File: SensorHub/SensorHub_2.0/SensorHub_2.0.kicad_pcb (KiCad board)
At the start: 2 copper layers, 30 x 28 mm, 68 parts, among them J1 Conn_01x02, J2 658561423020, J3 658561423020, J4 USB_C_Receptacle, U1 R7FA4E2B93CFM#AA0, U2 MYRGM080200C41RA, U3 TJA1051TK-3, U4 BMI270, U5 ASCODV-24.000MHZ-LR-T3

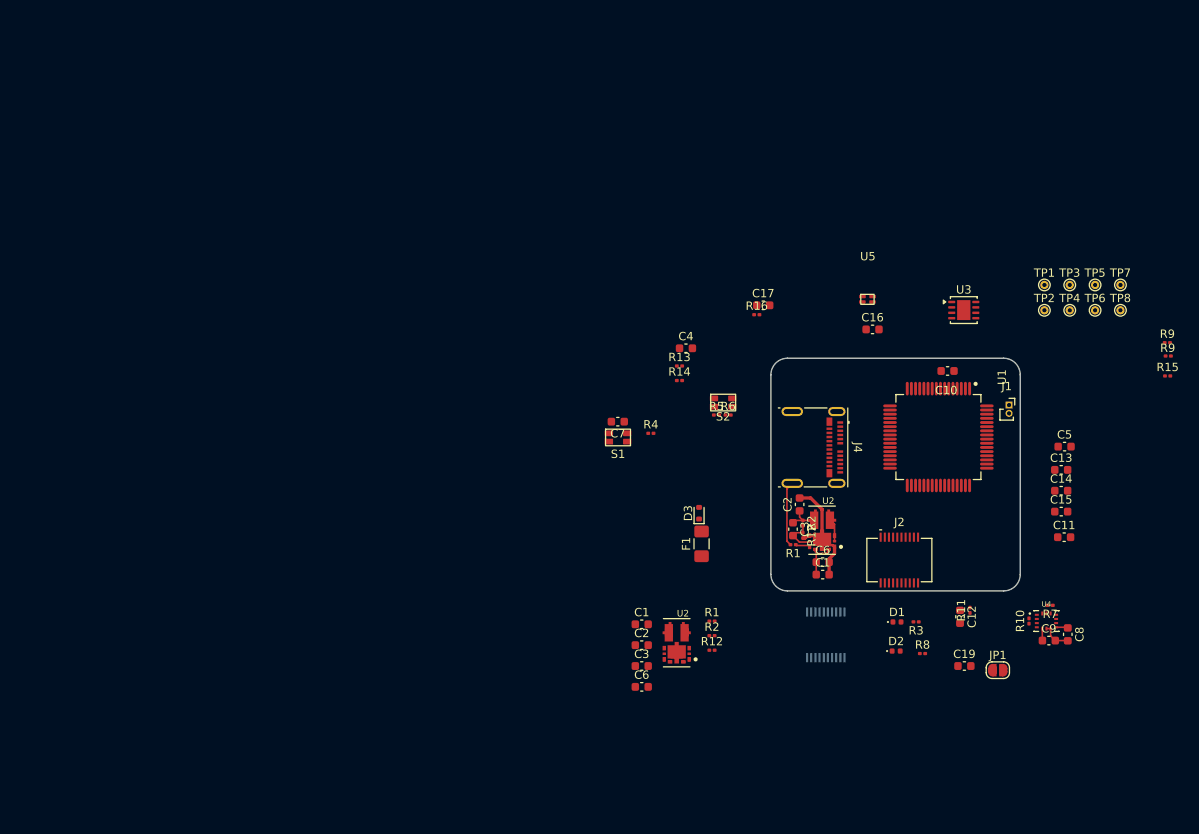
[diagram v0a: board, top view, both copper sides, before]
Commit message: 32k oscillator
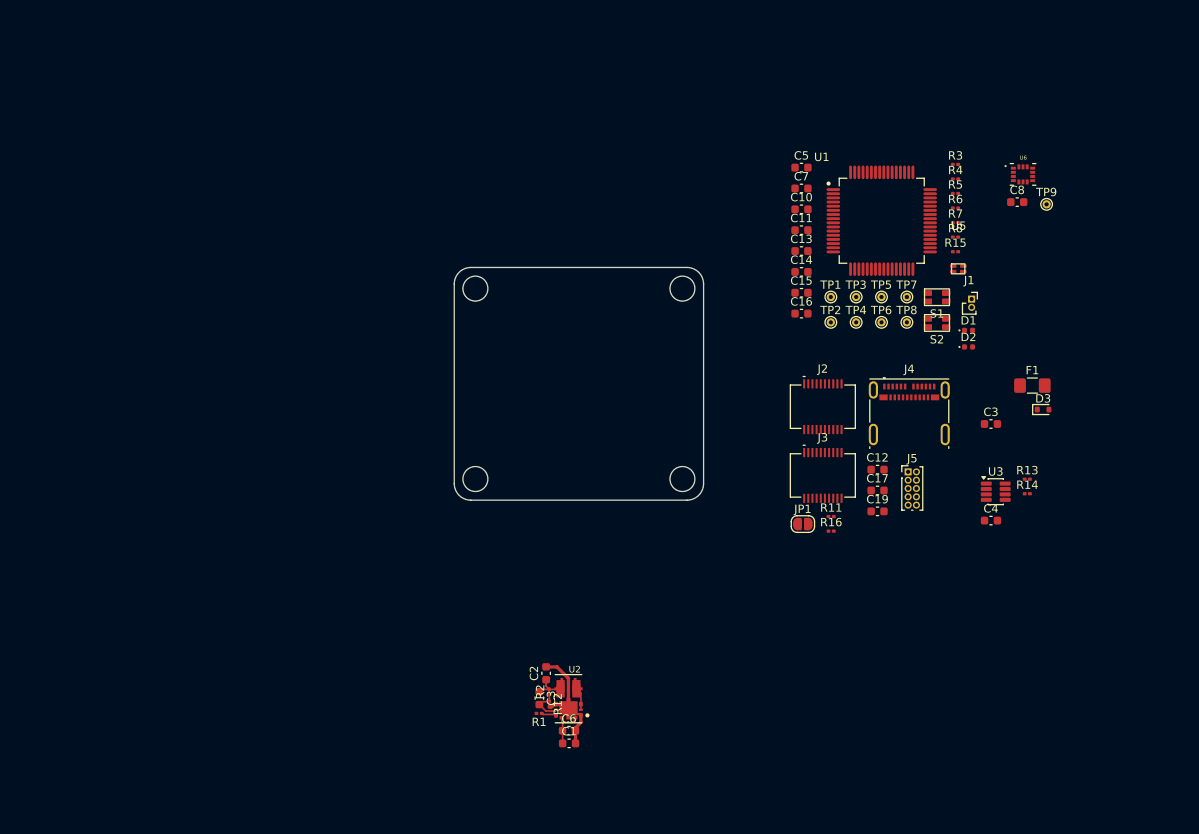
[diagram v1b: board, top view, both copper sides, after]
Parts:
- removed the C1 at (109.4, 129.6)
- removed the C1 at (131.2, 123.6)
- removed the C2 at (109.4, 132.1)
- removed the C2 at (128.4, 115.2)
- removed the C6 at (131.2, 122.1)
- removed the C6 at (109.4, 137.1)
- removed C9: 0.1 uF, Capacitor_SMD:C_0603_1608Metric
- removed the R1 at (127.6, 120.0)
- removed the R1 at (117.9, 129.2)
- removed R10, R9 (x2): 4.7 K, Resistor_SMD:R_0201_0603Metric
- removed the R12 at (117.9, 132.7)
- removed the R12 at (128.8, 118.9)
- removed the R2 at (117.9, 130.9)
- removed the R2 at (128.8, 117.4)
- removed the U2 at (131.1, 118.3)
- removed U4: BMI270, BMI270:XDCR_BMI270
- added C1: 10V/22uF, Capacitor_SMD:C_0603_1608Metric, F.Cu at (100.7, 143.9)
- added C2: 10V/22uF, Capacitor_SMD:C_0603_1608Metric, F.Cu at (97.9, 135.5)
- added C6: 16V/1uF, Capacitor_SMD:C_0603_1608Metric, F.Cu at (100.7, 142.4)
- added J5: Conn_02x05_Top_Bottom, Connector_PinHeader_1.00mm:PinHeader_2x05_P1.00mm_Vertical, F.Cu at (141.5, 111.2)
- added R1: 10 K, Resistor_SMD:R_0201_0603Metric, F.Cu at (97.1, 140.3)
- added R12: 15 K, Resistor_SMD:R_0201_0603Metric, F.Cu at (98.3, 139.2)
- added R2: 47 K, Resistor_SMD:R_0201_0603Metric, F.Cu at (98.3, 137.7)
- added TP9: TestPoint, TestPoint:TestPoint_THTPad_D1.0mm_Drill0.5mm, F.Cu at (158.1, 79.0)
- added U6: LSM6DSM, LSM6DSM:PQFN50P300X250X86-14N, F.Cu at (155.3, 75.5)
- J3: moved to F.Cu
- U3: value TJA1051TK-3 -> TCAN334; footprint Package_SON:HVSON-8-1EP_3x3mm_P0.65mm_EP1.6x2.4mm -> Package_TO_SOT_SMD:TSOT-23-8
- moved R3 55.2 mm to (147.2, 74.2), turned to 0 degrees
- moved C8 52.4 mm to (154.6, 78.8), turned to 0 degrees
- moved C3 51.1 mm to (151.4, 105.5)
- moved R8 50.3 mm to (147.2, 83.0)
- moved C11 48.6 mm to (128.6, 82.2)
- moved R4 47.7 mm to (147.2, 76.0)
- moved R7 47.4 mm to (147.2, 81.2), turned to 0 degrees
- moved C5 46.1 mm to (128.6, 74.6)
- moved F1 44.1 mm to (156.4, 100.9), turned to 0 degrees
- moved R13 44.0 mm to (155.8, 112.1)
- moved R14 44.0 mm to (155.8, 113.9)
- moved D3 43.2 mm to (157.7, 103.7), turned to 0 degrees
- moved C4 42.2 mm to (151.4, 117.1)
- moved S1 41.9 mm to (144.9, 89.7)
- moved C13 40.9 mm to (128.6, 84.7)
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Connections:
- net /Boot renamed /RA4E2_microcontroller/Boot
- net /EXTAL renamed /RA4E2_microcontroller/EXTAL
- net /LED1 renamed /RA4E2_microcontroller/LED1
- net /LED2 renamed /RA4E2_microcontroller/LED2
- net /SWCLK renamed /RA4E2_microcontroller/SWCLK
- net /SWDIO renamed /RA4E2_microcontroller/SWDIO
- net /VCL renamed /RA4E2_microcontroller/VCL
- C16 pad 1: +3.3V -> unconnected-(C16-Pad1)
- C4 pad 2: unconnected-(C4-Pad2) -> GND
- J2 pad 1: unconnected-(J2-Pad1) -> GND
- J2 pad 10: unconnected-(J2-Pad10) -> GND
- J2 pad 11: unconnected-(J2-Pad11) -> GND
- J2 pad 12: unconnected-(J2-Pad12) -> /SCL_0
- J2 pad 13: unconnected-(J2-Pad13) -> GND
- J2 pad 14: unconnected-(J2-Pad14) -> /SDA_0
- J2 pad 15: unconnected-(J2-Pad15) -> GND
- J2 pad 16: unconnected-(J2-Pad16) -> /CS
- J2 pad 17: unconnected-(J2-Pad17) -> /SCK
- J2 pad 18: unconnected-(J2-Pad18) -> /MOSI
- J2 pad 19: unconnected-(J2-Pad19) -> /MISO
- J2 pad 2: unconnected-(J2-Pad2) -> /+3.3V
- J2 pad 20: unconnected-(J2-Pad20) -> GND
- J2 pad 3: unconnected-(J2-Pad3) -> GND
- J2 pad 4: unconnected-(J2-Pad4) -> /Analog
- J2 pad 5: unconnected-(J2-Pad5) -> GND
- J2 pad 6: unconnected-(J2-Pad6) -> /INT2
- J2 pad 7: unconnected-(J2-Pad7) -> /GP1
- J2 pad 8: unconnected-(J2-Pad8) -> GND
- J2 pad 9: unconnected-(J2-Pad9) -> /+5V
- J3 pad 1: unconnected-(J3-Pad1) -> GND
- J3 pad 10: unconnected-(J3-Pad10) -> GND
- J3 pad 11: unconnected-(J3-Pad11) -> GND
- J3 pad 12: unconnected-(J3-Pad12) -> /SCL_0
- J3 pad 13: unconnected-(J3-Pad13) -> GND
- J3 pad 14: unconnected-(J3-Pad14) -> /SDA_0
- J3 pad 15: unconnected-(J3-Pad15) -> GND
- J3 pad 16: unconnected-(J3-Pad16) -> /CS
- J3 pad 17: unconnected-(J3-Pad17) -> /SCK
- J3 pad 18: unconnected-(J3-Pad18) -> /MOSI
- J3 pad 19: unconnected-(J3-Pad19) -> /MISO
- J3 pad 2: unconnected-(J3-Pad2) -> /+3.3V
- J3 pad 20: unconnected-(J3-Pad20) -> GND
- J3 pad 3: unconnected-(J3-Pad3) -> GND
- J3 pad 4: unconnected-(J3-Pad4) -> /Analog
- J3 pad 5: unconnected-(J3-Pad5) -> GND
- J3 pad 6: unconnected-(J3-Pad6) -> /INT2
- J3 pad 7: unconnected-(J3-Pad7) -> /GP1
- J3 pad 8: unconnected-(J3-Pad8) -> GND
- J3 pad 9: unconnected-(J3-Pad9) -> /+5V
- R15 pad 2: /SDA_0 -> /SDL_0
- TP4 pad 1: /SDA_0 -> /SDL_0
- U1 pad 12: /TX+ -> unconnected-(U1-P411-Pad12)
- U1 pad 14: /GPIO -> /GP1
- U1 pad 28: /INT2 -> unconnected-(U1-P304-Pad28)
- U1 pad 34: /MISO/SCL -> /MISO
- U1 pad 35: /MOSI/SDA -> /MOSI
- U1 pad 4: /SDA_0 -> /SDL_0
- U2 pad 6: /MYRGM080200C41RA +5\+3.3/Sleep -> /Sleep
- U3 pad 2: Net-(U3-GND-Pad2) -> GND
- U3 pad 3: +5V -> +3.3V
- U3 pad 5: +3.3V -> GND
- U3 pad 8: unconnected-(U3-S-Pad8) -> GND
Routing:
- net GND: track 26.5 -> 16.9 mm
- net +3.3V: track 6.97 -> 4.09 mm
- net /MYRGM080200C41RA +5\+3.3/LX: track 0.00 -> 2.79 mm
- net /LX: track 2.79 -> 0.00 mm
- net unconnected-(U2-2_NC-Pad4): track 1.22 -> 0.00 mm
- net unconnected-(U2-1_NC-Pad1): track 0.68 -> 0.00 mm

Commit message: New_USB_2.0
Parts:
- removed the C3 at (97.1, 138.5)
- removed the C3 at (151.4, 105.5)
- removed D1, D2: LED, LED_SMD:LED_0402_1005Metric
- removed R3, R8: 1.33 K, Resistor_SMD:R_0201_0603Metric
- removed S1: Reset, Library:Button_Mini_2.5x1.7mm
- removed S2: Boot, Library:Button_Mini_2.5x1.7mm
- removed TP1, TP2, TP7: TestPoint, TestPoint:TestPoint_THTPad_D1.0mm_Drill0.5mm
- removed U5: ASCODV-24.000MHZ-LR-T3, Library:ASCODV-24.000MHZ-LR-T3
- added C3: 330 pF, Capacitor_SMD:C_0603_1608Metric, F.Cu at (71.7, 140.5)
- added C9: 0.1 uF, Capacitor_SMD:C_0603_1608Metric, F.Cu at (131.9, 62.5)
- added D4: 1312020030000, 1312020030000:1312020030000, F.Cu at (131.8, 64.8)
- added D5: 1312020030000, 1312020030000:1312020030000, F.Cu at (135.1, 64.8)
- added SW1: SW_Push, Library:B3U-1000P(M)-B, F.Cu at (89.1, 62.4)
- added SW2: SW_Push, Library:B3U-1000P(M)-B, F.Cu at (101.9, 62.5)
- added U4: USBLC6-4SC6, Package_TO_SOT_SMD:SOT-23-6, F.Cu at (51.9, 79.3)
- added U7: USBLC6-4SC6, Package_TO_SOT_SMD:SOT-23-6, F.Cu at (51.9, 84.0)
- added Y1: ASH7KW-32.768KHZ-L-T, ASH7KW-32.768KHZ-L-T:XTAL_ASH7KW-32.768KHZ-L-T, F.Cu at (68.6, 65.0)
- J1: value Conn_01x02 -> USB_C_Receptacle; footprint Connector_PinSocket_1.00mm:PinSocket_1x02_P1.00mm_Vertical -> Connector_USB:USB_C_Receptacle_Molex_105450-0101
- J3: moved to B.Cu
- J5: value Conn_02x05_Top_Bottom -> FTSH-105-01-L-DV-K-A; footprint Connector_PinHeader_1.00mm:PinHeader_2x05_P1.00mm_Vertical -> FTSH-105-01-L-DV-K-A:SAMTEC_FTSH-105-01-L-DV-K-A
- moved J1 110.8 mm to (38.5, 97.0), turned to -90 degrees
- moved F1 95.3 mm to (63.6, 122.7)
- moved D3 95.2 mm to (64.8, 124.6), turned to 180 degrees
- moved R7 87.1 mm to (90.9, 147.8)
- moved R15 85.8 mm to (90.9, 149.5)
- moved J4 84.6 mm to (57.1, 108.9)
- moved C16 64.9 mm to (68.4, 67.9)
- moved R4 56.7 mm to (92.0, 63.0), turned to 180 degrees
- moved R5 51.0 mm to (98.7, 61.9)
- moved R6 51.0 mm to (98.7, 63.6)
- moved J5 50.7 mm to (168.7, 68.5)
- moved J2 45.6 mm to (105.9, 141.4)
- moved C7 39.1 mm to (92.6, 61.9)
- moved J3 39.0 mm to (105.9, 141.4), turned to 180 degrees
- moved C19 38.4 mm to (120.5, 150.3)
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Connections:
- C15 pad 1: +3.3V -> Net-(C15-Pad1)
- C16 pad 1: unconnected-(C16-Pad1) -> +3.3V
- J4 pad A10: /Can_H -> /USB_C/Can_H
- J4 pad A11: /Can_L -> /USB_C/Can_L
- J4 pad A2: /TX+ -> /USB_C/TX+
- J4 pad A3: /RES_usb -> /USB_C/TX-
- J4 pad A4: /V_Bus -> /USB_C/V_Bus
- J4 pad A6: /USB_DP -> /USB_C/USB_DP
- J4 pad A7: /USB_DM -> /USB_C/USB_DM
- J4 pad A8: /Sleep -> /USB_C/Sleep
- J4 pad A9: /V_Bus -> /USB_C/V_Bus
- J4 pad B10: /Can_H -> /USB_C/Can_H
- J4 pad B11: /Can_L -> /USB_C/Can_L
- J4 pad B2: /TX+ -> /USB_C/TX+
- J4 pad B3: /RES_usb -> /USB_C/TX-
- J4 pad B4: /V_Bus -> /USB_C/V_Bus
- J4 pad B6: /USB_DP -> /USB_C/USB_DP
- J4 pad B7: /USB_DM -> /USB_C/USB_DM
- J4 pad B8: /Sleep -> /USB_C/Sleep
- J4 pad B9: /V_Bus -> /USB_C/V_Bus
- J5 pad 10: unconnected-(J5-Pin_10-Pad10) -> /RES
- TP8 pad 1: /TX+ -> /TXD
- U1 pad 22: /RA4E2_microcontroller/LED2 -> unconnected-(U1-P206-Pad22)
- U1 pad 27: /RA4E2_microcontroller/LED1 -> /RA4E2_microcontroller/LED
- U1 pad 47: /TX+ -> /TXD
- U3 pad 1: /TX+ -> /TXD
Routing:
- net (no net): track 0.00 -> 1.50 mm, vias 0 -> 1
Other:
- copper layers 2 -> 4

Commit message: PCB 1st upd
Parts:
- removed J1, J4: USB_C_Receptacle, Connector_USB:USB_C_Receptacle_Molex_105450-0101
- added C18: 0.1 uF, Capacitor_SMD:C_0603_1608Metric, B.Cu at (106.5, 95.6)
- added C20: 0.1 uF, Capacitor_SMD:C_0603_1608Metric, F.Cu at (83.6, 103.7)
- added C21: 0.1 uF, Capacitor_SMD:C_0603_1608Metric, F.Cu at (83.6, 97.3)
- added J6: USB_C_Receptacle_USB2.0_16P, Connector_USB:USB_C_Receptacle_Palconn_UTC16-G, B.Cu at (78.7, 100.7)
- added J8: USB_C_Receptacle_USB2.0_16P, Connector_USB:USB_C_Receptacle_Palconn_UTC16-G, F.Cu at (78.7, 100.7)
- added R10: 5.1 K, Resistor_SMD:R_0201_0603Metric, F.Cu at (45.9, 116.2)
- added R3: 100 K, Resistor_SMD:R_0201_0603Metric, F.Cu at (44.2, 110.0)
- added R8: 5.1 K, Resistor_SMD:R_0201_0603Metric, F.Cu at (44.2, 110.7)
- added R9: 5.1 K, Resistor_SMD:R_0201_0603Metric, F.Cu at (44.5, 116.2)
- added TP1: TestPoint, TestPoint:TestPoint_THTPad_D1.0mm_Drill0.5mm, F.Cu at (117.0, 75.5)
- added TP2: TestPoint, TestPoint:TestPoint_THTPad_D1.0mm_Drill0.5mm, F.Cu at (117.0, 67.5)
- added TP7: TestPoint, TestPoint:TestPoint_THTPad_D1.0mm_Drill0.5mm, F.Cu at (117.0, 70.5)
- added U10: LMV339, Package_SO:SOIC-14_3.9x8.7mm_P1.27mm, F.Cu at (49.3, 100.6)
- added U5: TMUX154EDGS, Package_SO:VSSOP-10_3x3mm_P0.5mm, F.Cu at (62.5, 132.2)
- C10, C11, C13, C14, C17, U4, U7: moved to B.Cu
- moved J5 86.2 mm to (93.6, 110.6)
- moved TP9 53.3 mm to (117.1, 72.5)
- moved C17 53.2 mm to (98.7, 94.7), turned to 90 degrees
- moved R11 52.8 mm to (137.4, 102.5), turned to -90 degrees
- moved C19 49.7 mm to (135.6, 103.0)
- moved R14 49.4 mm to (88.4, 127.6), turned to 180 degrees
- moved R13 49.2 mm to (88.4, 126.9), turned to 180 degrees
- moved U3 48.5 mm to (85.6, 126.5)
- moved C4 46.3 mm to (88.4, 125.0), turned to 90 degrees
- moved JP1 46.1 mm to (132.4, 102.5)
- moved U6 44.4 mm to (123.0, 115.5)
- moved C15 44.2 mm to (99.6, 89.0), turned to 90 degrees
- moved C12 44.2 mm to (135.6, 101.5), turned to 180 degrees
- moved C8 43.6 mm to (122.6, 117.8)
- moved C11 42.9 mm to (102.6, 101.9)
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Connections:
- C17 pad 1: /RES -> +3.3V
- J3 pad 12: /SCL_0 -> /+3.3V
- J3 pad 14: /SDA_0 -> /Analog
- J3 pad 16: /CS -> /INT2
- J3 pad 17: /SCK -> /GP1
- J3 pad 18: /MOSI -> GND
- J3 pad 19: /MISO -> /+5V
- J3 pad 2: /+3.3V -> /SCL_0
- J3 pad 4: /Analog -> /SDA_0
- J3 pad 6: /INT2 -> /CS
- J3 pad 7: /GP1 -> /SCK
- J3 pad 8: GND -> /MOSI
- J3 pad 9: /+5V -> /MISO
- J5 pad 02: /RA4E2_microcontroller/SWDIO -> /RA4E2_microcontroller/SWCLK
- J5 pad 04: /RA4E2_microcontroller/SWCLK -> /RA4E2_microcontroller/SWDIO
- R15 pad 2: /SDL_0 -> /SDA_0
- TP4 pad 1: /SDL_0 -> /SDA_0
- U1 pad 12: unconnected-(U1-P411-Pad12) -> /GP3
- U1 pad 13: unconnected-(U1-P410-Pad13) -> /GP2
- U1 pad 4: /SDL_0 -> /SDA_0
- U4 pad 1: /USB_C/USB_DM -> /USB_DM
- U4 pad 3: /USB_C/USB_DP -> /USB_DP
- U4 pad 4: /USB_C/Can_L -> /USB_C_2.0+SBUS/CC1
- U4 pad 5: /USB_C/V_Bus -> /V_Bus
- U4 pad 6: /USB_C/Can_H -> /USB_C_2.0+SBUS/CC2
- U7 pad 1: /USB_C/TXD -> /USB_C_2.0+SBUS/SBU1
- U7 pad 3: /USB_C/RES_usb -> /USB_C_2.0+SBUS/SBU2
- U7 pad 4: /USB_C/Sleep -> unconnected-(U7-I/O3-Pad4)
- U7 pad 5: /USB_C/V_Bus -> /V_Bus
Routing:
- net GND: track 16.9 -> 73.4 mm, vias 0 -> 11
- net /USB_DP: track 0.00 -> 6.55 mm, vias 0 -> 1
- net /USB_DM: track 0.00 -> 6.52 mm, vias 0 -> 1
- net /USB_C_2.0+SBUS/SBU2: track 0.00 -> 6.01 mm, vias 0 -> 1
- net /USB_C_2.0+SBUS/CC2: track 0.00 -> 5.97 mm, vias 0 -> 1
- net /USB_C_2.0+SBUS/CC1: track 0.00 -> 4.62 mm, vias 0 -> 1
- net /USB_C_2.0+SBUS/SBU1: track 0.00 -> 4.55 mm, vias 0 -> 1
- net /FB: track 4.54 -> 0.00 mm
- net /MYRGM080200C41RA +5\+3.3/FB: track 0.00 -> 4.54 mm
- net /RES: track 0.00 -> 2.68 mm
- net /SCK: track 0.00 -> 1.97 mm, vias 0 -> 1
- net /GP1: track 0.00 -> 1.96 mm, vias 0 -> 1
- net /MOSI: track 0.00 -> 1.96 mm, vias 0 -> 1
- net /CS: track 0.00 -> 1.94 mm, vias 0 -> 1
- net /SDA_0: track 0.00 -> 1.94 mm, vias 0 -> 1
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
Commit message: PCB upd 2
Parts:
- R15, R7, U10: moved to B.Cu
- U4, U7: moved to F.Cu
- moved R15 57.0 mm to (104.1, 94.0), turned to 90 degrees
- moved R7 56.5 mm to (104.9, 94.0), turned to 90 degrees
- moved R14 32.2 mm to (111.8, 105.6), turned to -90 degrees
- moved R13 31.2 mm to (111.1, 105.6), turned to -90 degrees
- moved U3 31.0 mm to (110.7, 108.4), turned to 90 degrees
- moved C5 30.6 mm to (108.4, 68.1)
- moved C4 28.5 mm to (109.3, 105.6), turned to 180 degrees
- moved R11 27.5 mm to (110.0, 104.0), turned to 180 degrees
- moved C19 26.1 mm to (109.5, 102.1), turned to -90 degrees
- moved R16 26.0 mm to (127.6, 99.8)
- moved IMU 25.5 mm to (110.5, 93.2)
- moved C8 24.7 mm to (110.2, 96.4)
- moved C12 24.6 mm to (111.0, 102.1), turned to 90 degrees
- moved JP1 22.7 mm to (110.0, 98.9), turned to -90 degrees
- moved TP2 20.6 mm to (125.2, 86.4)
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- renumbered U6 to IMU
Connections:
- D3 pad 1: Net-(D3-K) -> +5V
- D3 pad 2: /V_Bus -> Net-(D3-A)
- F1 pad 1: +5V -> Net-(D3-A)
- F1 pad 2: Net-(D3-K) -> /V_Bus
- IMU pad 14: /SDL_0 -> /SDA_0
- U1 pad 1: /INT2 -> /INT1
- U1 pad 44: /INT1 -> /INT2
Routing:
- net /V_Bus: track 0.00 -> 14.4 mm, vias 1 -> 0
- net +3.3V: track 5.41 -> 18.0 mm, vias 0 -> 7
- net /SDA_0: track 1.94 -> 12.2 mm, vias 1 -> 4
- net /SCL_0: track 1.94 -> 11.4 mm, vias 1 -> 2
- net GND: track 73.4 -> 78.7 mm, vias 11 -> 18
- net /RA4E2_microcontroller/EXTAL: track 0.00 -> 5.19 mm
- net /INT1: track 0.00 -> 4.97 mm
- net Net-(D3-A): track 0.00 -> 4.72 mm
- net /ADC/DA: track 0.00 -> 3.49 mm
- net /RA4E2_microcontroller/VCL: track 0.00 -> 2.34 mm, vias 0 -> 1
- net /Can_L: track 0.00 -> 1.71 mm, vias 0 -> 1
- net /Can_H: track 0.00 -> 1.69 mm, vias 0 -> 1
- net +5V: track 4.89 -> 6.51 mm
- net Net-(D4-Pad3): track 1.50 -> 0.00 mm
- net Net-(C9-Pad1): track 1.48 -> 0.00 mm
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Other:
- board text added: "Short JP1 and C19 for ADC"

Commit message: PCB_1.0
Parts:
- removed C5: 0.1 uF, Capacitor_SMD:C_0603_1608Metric
- removed R16: 1 K, Resistor_SMD:R_0201_0603Metric
- removed TP6, TP9: TestPoint, TestPoint:TestPoint_THTPad_D1.0mm_Drill0.5mm
- added EXTAL: TestPoint, TestPoint:TestPoint_THTPad_D1.0mm_Drill0.5mm, F.Cu at (163.6, 72.2)
- added FRAME1: FRAME-LEDGER, SensorHub MicroMod Carrier v1.1.0b:CREATIVE_COMMONS, F.Cu at (87.0, 123.7)
- added GND: TestPoint, TestPoint:TestPoint_THTPad_D1.0mm_Drill0.5mm, F.Cu at (148.6, 90.0)
- C4, R13, R14, U3: moved to B.Cu
- moved R9 95.5 mm to (145.8, 82.7)
- moved R3 93.4 mm to (145.8, 83.6)
- moved R8 93.4 mm to (145.8, 84.6)
- moved R10 92.7 mm to (143.6, 81.4), turned to 0 degrees
- moved U7 85.3 mm to (140.8, 79.9)
- moved U4 85.1 mm to (140.8, 84.3)
- moved U5 81.7 mm to (146.4, 79.5)
- moved U10 81.2 mm to (145.8, 83.3)
- moved C18 58.4 mm to (162.7, 79.8)
- moved C14 58.3 mm to (162.7, 83.0)
- moved R6 58.0 mm to (146.1, 71.5)
- moved R11 57.9 mm to (165.7, 88.1)
- moved J2 57.9 mm to (159.5, 94.4)
- moved J3 57.9 mm to (159.5, 94.4)
- moved Boot 57.8 mm to (144.8, 73.2)
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- renumbered SW2 to Boot, TP7 to GP2, TP2 to GP3, TP5 to RES, SW1 to RES, TP4 to SCL, TP3 to SDA, TP8 to TXD, IMU to U6, TP1 to |Boot
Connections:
- net /Sleep renamed Net-(U2-CE)
- J2 pad 9: /+5V -> +5V
- J3 pad 19: /+5V -> +5V
- R1 pad 2: GND -> +5V
- RES pad 1: /RA4E2_microcontroller/Boot -> /RES
- SCL pad 1: /SDA_0 -> /SCL_0
- SDA pad 1: /SCL_0 -> /SDA_0
- U1 pad 12: /GP3 -> unconnected-(U1-P411-Pad12)
- U1 pad 13: /GP2 -> unconnected-(U1-P410-Pad13)
- U1 pad 29: unconnected-(U1-P303-Pad29) -> /GP3
- U1 pad 30: unconnected-(U1-P302-Pad30) -> /GP2
- U1 pad 41: unconnected-(U1-P107-Pad41) -> /RA4E2_microcontroller/Sleep
- U4 pad 1: /USB_DM -> /USB_DP
- U4 pad 3: /USB_DP -> /USB_DM
- U4 pad 4: /USB_C_2.0+SBUS/CC1 -> /USB_C_2.0+SBUS/CC2
- U4 pad 6: /USB_C_2.0+SBUS/CC2 -> /USB_C_2.0+SBUS/CC1
- U7 pad 1: /USB_C_2.0+SBUS/SBU1 -> /USB_C_2.0+SBUS/SBU2
- U7 pad 3: /USB_C_2.0+SBUS/SBU2 -> /USB_C_2.0+SBUS/SBU1
- |Boot pad 1: /RES -> /RA4E2_microcontroller/Boot
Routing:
- net /RES: track 2.68 -> 36.9 mm, vias 0 -> 3
- net /USB_DM: track 6.52 -> 36.3 mm, vias 1 -> 5
- net /V_Bus: track 14.4 -> 42.7 mm, vias 0 -> 1
- net /USB_DP: track 6.55 -> 34.0 mm, vias 1 -> 4
- net GND: track 78.7 -> 106.1 mm, vias 18 -> 42
- net /GP1: track 1.96 -> 28.5 mm
- net /SDA_0: track 12.2 -> 36.5 mm
- net /SCL_0: track 11.4 -> 34.1 mm
- net +3.3V: track 18.0 -> 40.2 mm, vias 7 -> 17
- net +5V: track 6.51 -> 28.2 mm, vias 0 -> 2
- net /RA4E2_microcontroller/Boot: track 0.00 -> 20.9 mm, vias 1 -> 3
- net /USB_C_2.0+SBUS/SBU2: track 6.01 -> 26.3 mm, vias 1 -> 4
- net /USB_C_2.0+SBUS/SBU1: track 4.55 -> 22.8 mm, vias 1 -> 3
- net /USB_C_2.0+SBUS/CC1: track 4.62 -> 20.5 mm, vias 1 -> 2
- net /TXD: track 0.00 -> 15.0 mm, vias 0 -> 1
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- added copper zone on In2.Cu, net +3.3V
- added copper zone on In1.Cu, net GND
